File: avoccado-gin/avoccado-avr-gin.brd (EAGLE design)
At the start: 27 x 14.5 mm, 57 parts, among them Q1 16MHz, Q2 N-FET, U1 MPU-6000QFN-24, U2 MCP73831

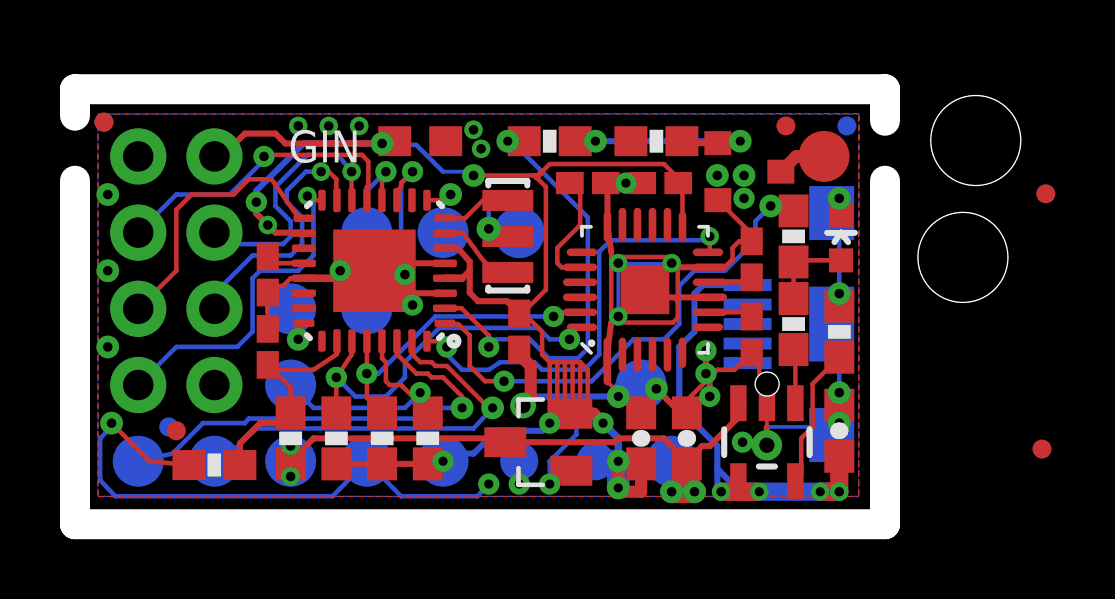
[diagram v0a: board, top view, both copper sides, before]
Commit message: Gin: fix mirrored silkscreen on bottom layer
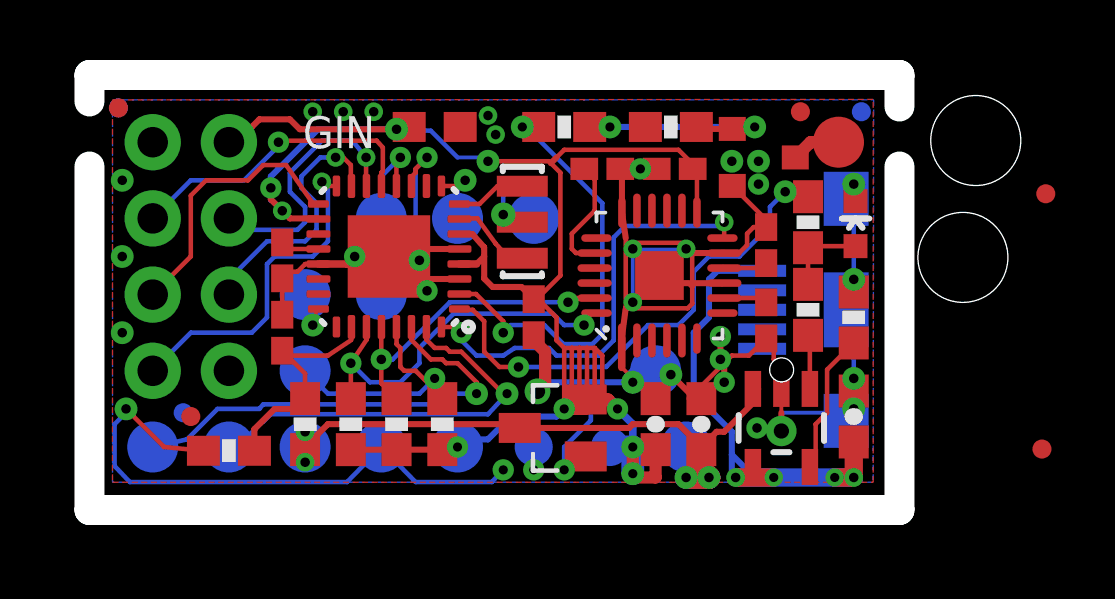
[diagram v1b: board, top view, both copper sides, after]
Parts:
- moved C2 0.68 mm to (19.5, 11.4)
- moved C9 0.68 mm to (17.1, 11.4)
- moved D1 0.68 mm to (25.5, 9.55)
- moved Q2 0.68 mm to (22.4, 11.8)
- moved C5 0.68 mm to (20.4, 2.86)
- moved TP4 0.68 mm to (19.9, 2.10)
- moved C10 0.68 mm to (11.5, 12.8)
- moved FID5 0.68 mm to (23.7, 13.3)
- moved FID9 0.68 mm to (25.7, 13.3)
- moved JP22 0.68 mm to (25.2, 6.67)
- moved JP27 0.68 mm to (2.11, 9.72)
- moved R1 0.68 mm to (15.8, 12.8)
- moved R4 0.68 mm to (24.0, 6.67)
- moved R6 0.68 mm to (24.0, 9.59)
- moved TP11 0.68 mm to (9.73, 9.72)
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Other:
- board text added: "OCC DO"

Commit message: add PCBs with ICSP adapters and panelize
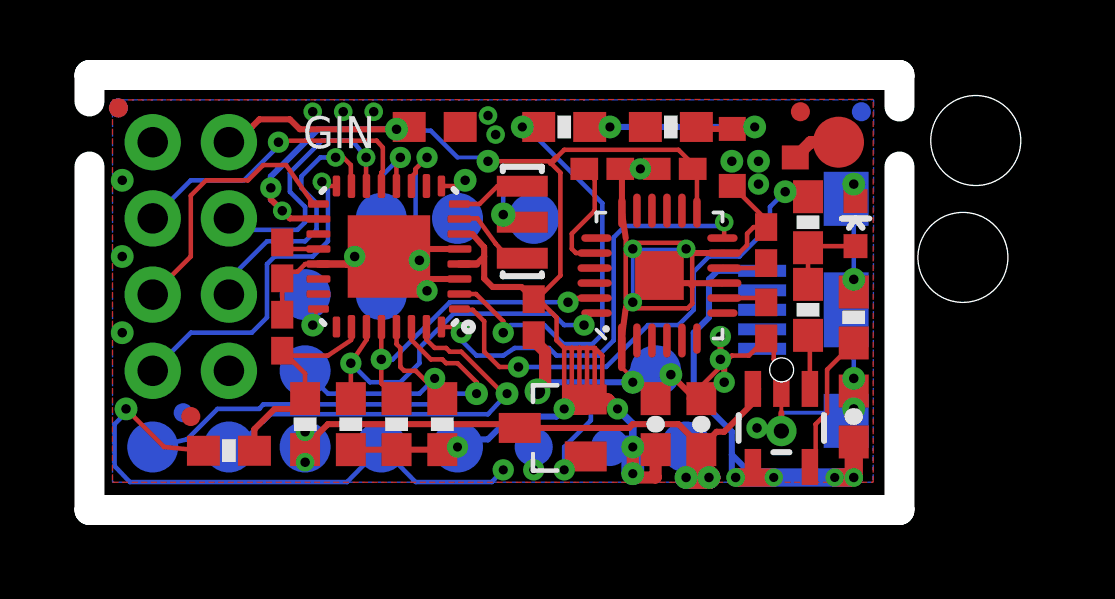
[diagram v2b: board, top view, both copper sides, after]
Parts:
- removed FID1, FID3: FIDUCIALUFIDUCIAL, SparkFun-Aesthetics:MICRO-FIDUCIAL
